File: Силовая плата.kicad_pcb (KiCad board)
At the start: 6 copper layers, 66 x 71.8 mm, 40 parts, among them J3 Conn_01x01, J4 Conn_01x01, J5 Conn_01x01, J6 Conn_01x04, J9 Conn_01x08, Q1 2N7002, Q2 2N7002, Q3 2N7002, Q4 2N7002, Q5 2N7002, Q6 2N7002, U1 AD8210, U2 AD8603, U3 AD8603, U4 AD8603

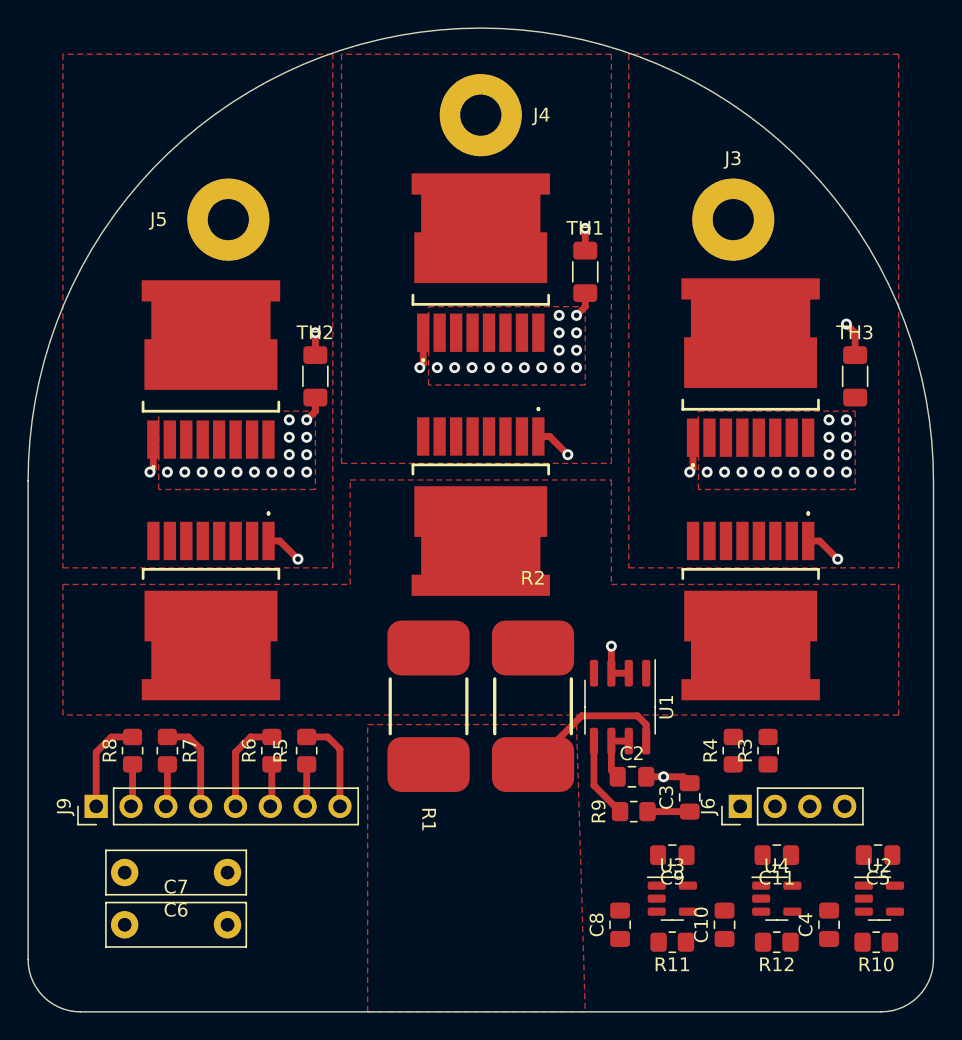
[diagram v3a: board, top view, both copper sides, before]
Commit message: Перенес защиту от переполюсовки и добавил керамику
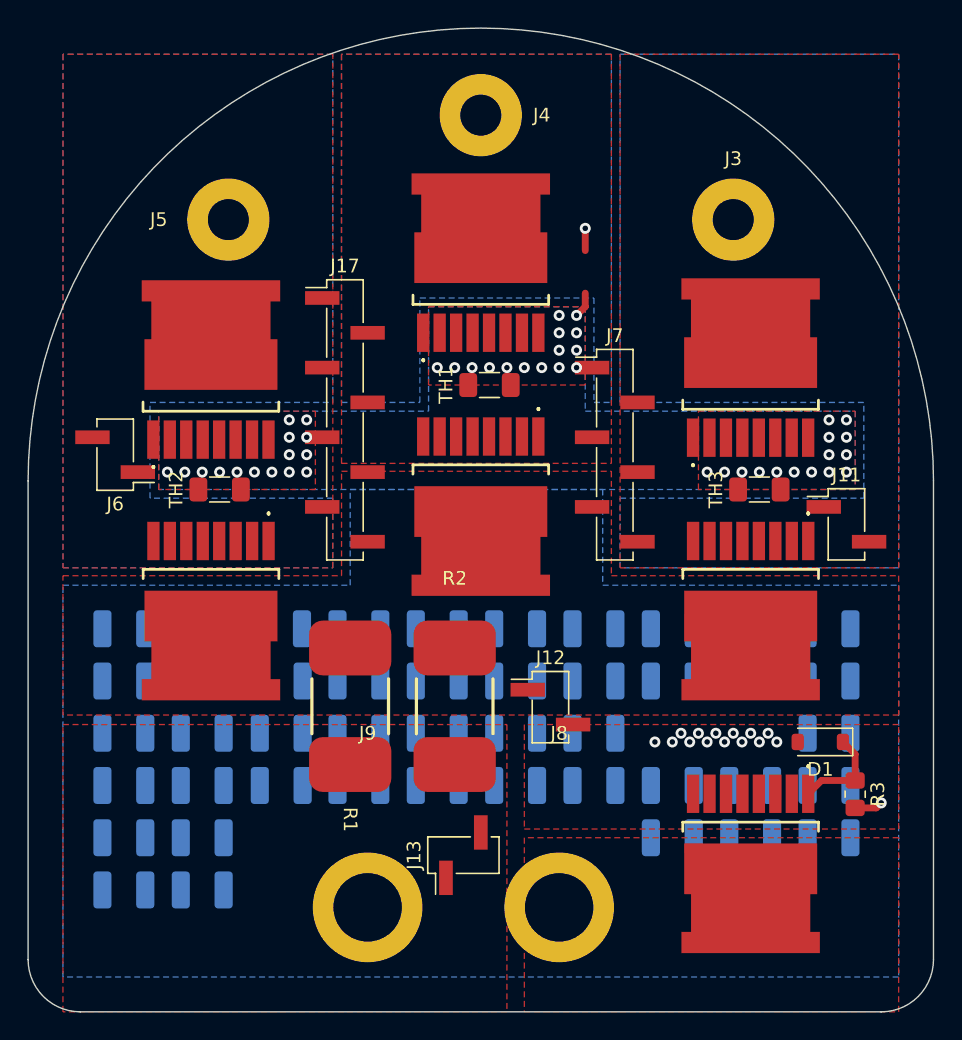
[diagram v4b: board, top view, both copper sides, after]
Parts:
- removed C6, C7: 1500p, Capacitor_THT:C_Rect_L10.0mm_W3.0mm_P7.50mm_FKS3_FKP3
- removed R10, R11, R12, R4, R5, R6, R7, R8: 10k, Resistor_SMD:R_0805_2012Metric_Pad1.20x1.40mm_HandSolder
- removed R9: 120, Resistor_SMD:R_0805_2012Metric_Pad1.20x1.40mm_HandSolder
- removed U1: AD8210, Package_SO:SOIC-8_3.9x4.9mm_P1.27mm
- removed U2, U3, U4: AD8603, Package_TO_SOT_SMD:TSOT-23-5
- added C1: 10u, Capacitor_SMD:C_1210_3225Metric_Pad1.33x2.70mm_HandSolder, B.Cu at (108.6, 120.7)
- added C12: 10u, Capacitor_SMD:C_1210_3225Metric_Pad1.33x2.70mm_HandSolder, B.Cu at (108.6, 116.8)
- added C13: 10u, Capacitor_SMD:C_1210_3225Metric_Pad1.33x2.70mm_HandSolder, B.Cu at (108.6, 109.2)
- added C14: 10u, Capacitor_SMD:C_1210_3225Metric_Pad1.33x2.70mm_HandSolder, B.Cu at (102.9, 109.2)
- added C15: 10u, Capacitor_SMD:C_1210_3225Metric_Pad1.33x2.70mm_HandSolder, B.Cu at (97.2, 120.7)
- added C16: 10u, Capacitor_SMD:C_1210_3225Metric_Pad1.33x2.70mm_HandSolder, B.Cu at (62.9, 124.5)
- added C17: 10u, Capacitor_SMD:C_1210_3225Metric_Pad1.33x2.70mm_HandSolder, B.Cu at (97.2, 109.2)
- added C18: 10u, Capacitor_SMD:C_1210_3225Metric_Pad1.33x2.70mm_HandSolder, B.Cu at (68.6, 105.4)
- added C19: 10u, Capacitor_SMD:C_1210_3225Metric_Pad1.33x2.70mm_HandSolder, B.Cu at (68.6, 109.2)
- added C20: 10u, Capacitor_SMD:C_1210_3225Metric_Pad1.33x2.70mm_HandSolder, B.Cu at (68.6, 113.0)
- added C21: 10u, Capacitor_SMD:C_1210_3225Metric_Pad1.33x2.70mm_HandSolder, B.Cu at (91.4, 109.2)
- added C22: 10u, Capacitor_SMD:C_1210_3225Metric_Pad1.33x2.70mm_HandSolder, B.Cu at (91.4, 105.4)
- added C23: 10u, Capacitor_SMD:C_1210_3225Metric_Pad1.33x2.70mm_HandSolder, B.Cu at (102.9, 105.4)
- added C24: 10u, Capacitor_SMD:C_1210_3225Metric_Pad1.33x2.70mm_HandSolder, B.Cu at (85.7, 105.4)
- added C25: 10u, Capacitor_SMD:C_1210_3225Metric_Pad1.33x2.70mm_HandSolder, B.Cu at (80.0, 105.4)
- added C26: 10u, Capacitor_SMD:C_1210_3225Metric_Pad1.33x2.70mm_HandSolder, B.Cu at (57.1, 124.5)
- added C27: 10u, Capacitor_SMD:C_1210_3225Metric_Pad1.33x2.70mm_HandSolder, B.Cu at (62.9, 116.8)
- added C28: 10u, Capacitor_SMD:C_1210_3225Metric_Pad1.33x2.70mm_HandSolder, B.Cu at (62.9, 113.0)
- added C29: 10u, Capacitor_SMD:C_1210_3225Metric_Pad1.33x2.70mm_HandSolder, B.Cu at (57.1, 120.7)
- added C30: 10u, Capacitor_SMD:C_1210_3225Metric_Pad1.33x2.70mm_HandSolder, B.Cu at (91.4, 116.8)
- added C31: 10u, Capacitor_SMD:C_1210_3225Metric_Pad1.33x2.70mm_HandSolder, B.Cu at (74.3, 113.0)
- added C32: 10u, Capacitor_SMD:C_1210_3225Metric_Pad1.33x2.70mm_HandSolder, B.Cu at (74.3, 116.8)
- added C33: 10u, Capacitor_SMD:C_1210_3225Metric_Pad1.33x2.70mm_HandSolder, B.Cu at (102.9, 116.8)
- added C34: 10u, Capacitor_SMD:C_1210_3225Metric_Pad1.33x2.70mm_HandSolder, B.Cu at (85.7, 116.8)
- added C35: 10u, Capacitor_SMD:C_1210_3225Metric_Pad1.33x2.70mm_HandSolder, B.Cu at (85.7, 113.0)
- added C36: 10u, Capacitor_SMD:C_1210_3225Metric_Pad1.33x2.70mm_HandSolder, B.Cu at (85.7, 109.2)
- added C37: 10u, Capacitor_SMD:C_1210_3225Metric_Pad1.33x2.70mm_HandSolder, B.Cu at (108.6, 105.4)
- added C38: 10u, Capacitor_SMD:C_1210_3225Metric_Pad1.33x2.70mm_HandSolder, B.Cu at (68.6, 116.8)
- added C39: 10u, Capacitor_SMD:C_1210_3225Metric_Pad1.33x2.70mm_HandSolder, B.Cu at (57.1, 116.8)
- added C40: 10u, Capacitor_SMD:C_1210_3225Metric_Pad1.33x2.70mm_HandSolder, B.Cu at (62.9, 105.4)
- added C41: 10u, Capacitor_SMD:C_1210_3225Metric_Pad1.33x2.70mm_HandSolder, B.Cu at (91.4, 113.0)
- added C42: 10u, Capacitor_SMD:C_1210_3225Metric_Pad1.33x2.70mm_HandSolder, B.Cu at (80.0, 113.0)
- added C43: 10u, Capacitor_SMD:C_1210_3225Metric_Pad1.33x2.70mm_HandSolder, B.Cu at (80.0, 116.8)
- added C44: 10u, Capacitor_SMD:C_1210_3225Metric_Pad1.33x2.70mm_HandSolder, B.Cu at (62.9, 120.7)
- added C45: 10u, Capacitor_SMD:C_1210_3225Metric_Pad1.33x2.70mm_HandSolder, B.Cu at (80.0, 109.2)
- added C46: 10u, Capacitor_SMD:C_1210_3225Metric_Pad1.33x2.70mm_HandSolder, B.Cu at (57.1, 113.0)
- added C47: 10u, Capacitor_SMD:C_1210_3225Metric_Pad1.33x2.70mm_HandSolder, B.Cu at (97.2, 105.4)
- added D1: BZT52C10, Diode_SMD:D_SOD-123, F.Cu at (108.0, 113.7)
- added J11: Conn_01x02, Connector_PinHeader_2.54mm:PinHeader_1x02_P2.54mm_Vertical_SMD_Pin1Left, F.Cu at (109.9, 97.8)
- added J12: Conn_01x02, Connector_PinHeader_2.54mm:PinHeader_1x02_P2.54mm_Vertical_SMD_Pin1Left, F.Cu at (88.3, 111.1)
- added J13: Conn_01x02, Connector_PinHeader_2.54mm:PinHeader_1x02_P2.54mm_Vertical_SMD_Pin1Left, F.Cu at (81.9, 121.9)
- added J17: Conn_01x08, Connector_PinHeader_2.54mm:PinHeader_1x08_P2.54mm_Vertical_SMD_Pin1Left, F.Cu at (73.3, 90.2)
- added J7: Conn_01x06, Connector_PinHeader_2.54mm:PinHeader_1x06_P2.54mm_Vertical_SMD_Pin1Left, F.Cu at (93.0, 92.7)
- added J8: IN-, Connector_My:Power_Wire, F.Cu at (88.9, 113.5)
- added Q7: BSS214NW, MOSFET_My:IPTG007N06NM5ATMA1, F.Cu at (102.9, 123.8)
- C10, C11, C4, C5, C8, C9: value 100n -> 10u; footprint Capacitor_SMD:C_0805_2012Metric_Pad1.18x1.45mm_HandSolder -> Capacitor_SMD:C_1210_3225Metric_Pad1.33x2.70mm_HandSolder; moved to B.Cu
- C2: value 0.1u -> 10u; footprint Capacitor_SMD:C_0805_2012Metric_Pad1.18x1.45mm_HandSolder -> Capacitor_SMD:C_1210_3225Metric_Pad1.33x2.70mm_HandSolder; moved to B.Cu
- C3: value 56p -> 10u; footprint Capacitor_SMD:C_0805_2012Metric_Pad1.18x1.45mm_HandSolder -> Capacitor_SMD:C_1210_3225Metric_Pad1.33x2.70mm_HandSolder; moved to B.Cu
- J6: value Conn_01x04 -> Conn_01x02; footprint Connector_PinHeader_2.54mm:PinHeader_1x04_P2.54mm_Vertical -> Connector_PinHeader_2.54mm:PinHeader_1x02_P2.54mm_Vertical_SMD_Pin1Left
- J9: value Conn_01x08 -> IN+; footprint Connector_PinHeader_2.54mm:PinHeader_1x08_P2.54mm_Vertical -> Connector_My:Power_Wire
- R3: value 10k -> 100k
- moved J6 52.3 mm to (56.5, 92.7), turned to 180 degrees
- moved C4 40.5 mm to (74.3, 105.4), turned to 0 degrees
- moved C8 40.3 mm to (57.1, 109.2), turned to 180 degrees
- moved C2 38.6 mm to (57.1, 105.4), turned to 180 degrees
- moved C3 36.6 mm to (62.9, 109.2), turned to 0 degrees
- moved C11 33.0 mm to (74.3, 109.2), turned to 0 degrees
- moved J9 20.4 mm to (74.9, 113.5), turned to 0 degrees
- moved C10 15.9 mm to (108.6, 113.0), turned to 0 degrees
- moved TH1 10.8 mm to (83.8, 87.6), turned to 0 degrees
- moved TH2 10.8 mm to (64.1, 95.2), turned to 0 degrees
- moved TH3 10.8 mm to (103.5, 95.2), turned to 0 degrees
- moved C5 9.38 mm to (102.9, 120.7)
- moved R3 7.10 mm to (110.5, 117.5), turned to -90 degrees
- moved R1 5.72 mm to (73.7, 106.8)
- moved R2 5.72 mm to (81.3, 106.8)
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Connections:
- C10 pad 1: Net-(U4-+) -> Shunt_1
- C11 pad 1: +5V -> Shunt_1
- C2 pad 1: +5V -> Shunt_1
- C3 pad 1: DC_Measure -> Shunt_1
- C4 pad 1: Net-(U2-+) -> Shunt_1
- C5 pad 1: +5V -> Shunt_1
- C8 pad 1: Net-(U3-+) -> Shunt_1
- C9 pad 1: +5V -> Shunt_1
- J6 pad 1: G1 -> G6
- J6 pad 2: A -> GND
- J9 pad 1: G6 -> Shunt_1
- R3 pad 1: A -> Net-(D1-K)
- R3 pad 2: G1 -> Shunt_1
- TH1 pad 1: Net-(U2-+) -> Temp_A
- TH2 pad 1: Net-(U3-+) -> Temp_C
- TH3 pad 1: Net-(U4-+) -> Temp_B
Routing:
- net G4: track 36.5 -> 0.00 mm, vias 1 -> 0
- net G6: track 29.1 -> 0.00 mm, vias 1 -> 0
- net G3: track 25.8 -> 0.00 mm, vias 1 -> 0
- net G2: track 21.8 -> 0.00 mm, vias 1 -> 0
- net G5: track 18.4 -> 0.00 mm, vias 1 -> 0
- net G1: track 15.0 -> 0.00 mm, vias 1 -> 0
- net GND: track 16.6 -> 1.89 mm, vias 47 -> 59
- net Shunt_1: track 11.2 -> 2.06 mm, vias 0 -> 1
- net Net-(D1-K): track 0.00 -> 7.00 mm
- net B: track 6.97 -> 0.00 mm
- net C: track 6.97 -> 0.00 mm
- net Net-(U1-OUT): track 5.93 -> 0.00 mm
- net +5V: track 4.07 -> 0.00 mm
- net DC_Measure: track 3.08 -> 0.00 mm
- net Net-(U4-+): track 2.52 -> 0.00 mm, vias 1 -> 0
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- added copper zone on B.Cu, net A
- added copper zone on B.Cu, net B
- added copper zone on B.Cu, net C
- added copper zone on B.Cu, net GND
- added copper zone on F.Cu, net Net-(J8-Pin_1)

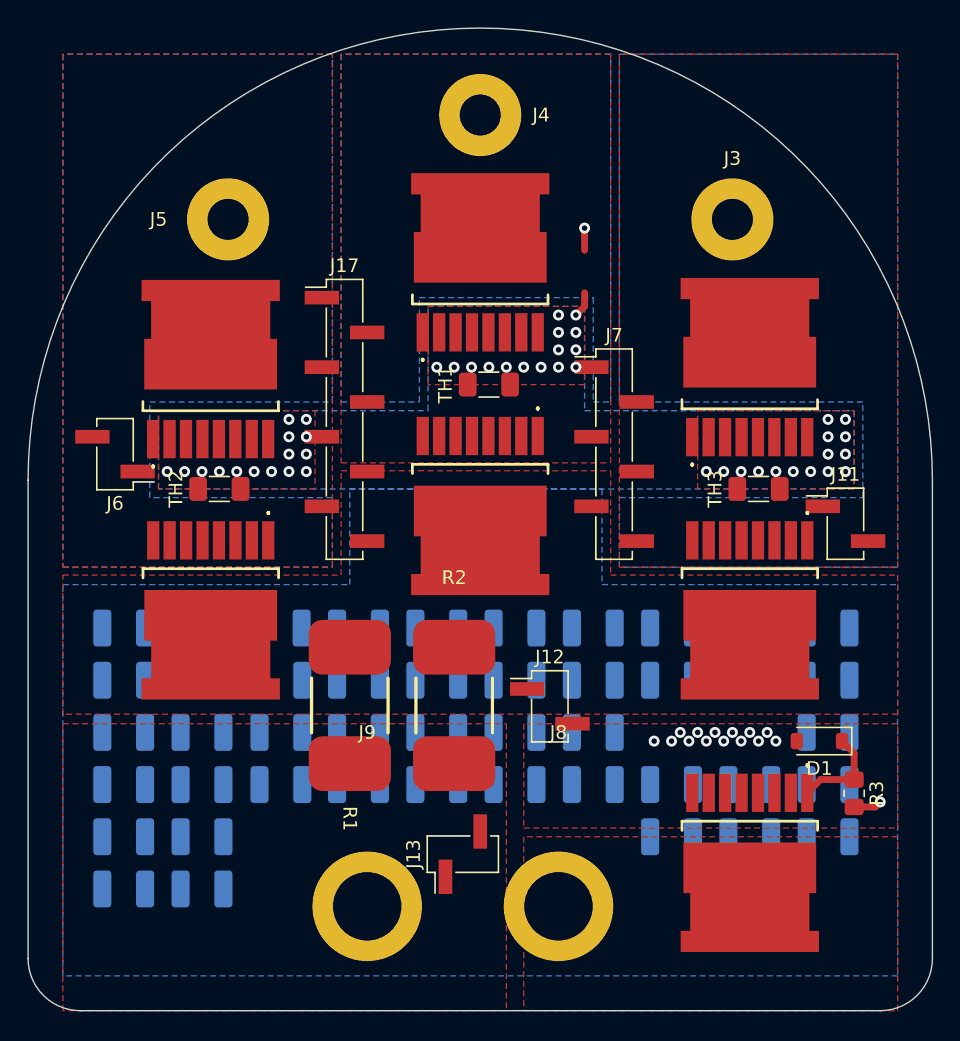
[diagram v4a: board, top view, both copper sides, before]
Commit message: Поставил керамические Y конденсаторы
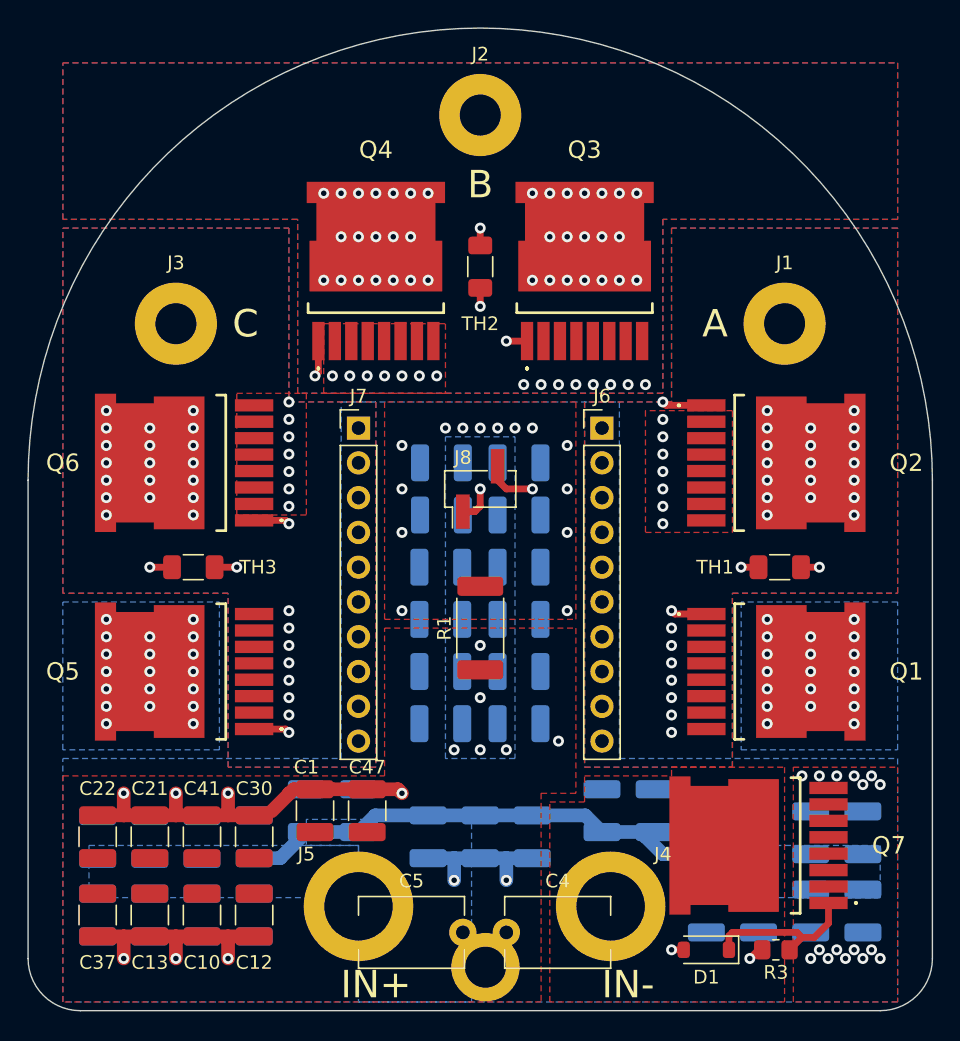
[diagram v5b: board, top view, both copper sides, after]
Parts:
- removed J11, J12: Conn_01x02, Connector_PinHeader_2.54mm:PinHeader_1x02_P2.54mm_Vertical_SMD_Pin1Left
- removed J17: Conn_01x08, Connector_PinHeader_2.54mm:PinHeader_1x08_P2.54mm_Vertical_SMD_Pin1Left
- removed R2: R, Shunt_My:TLRS1050
- added C4: 1500p, Capacitor_THT:C_Disc_D7.5mm_W5.0mm_P7.50mm, F.Cu at (85.1, 127.6)
- added C5: 1500p, Capacitor_THT:C_Disc_D7.5mm_W5.0mm_P7.50mm, F.Cu at (74.4, 127.6)
- added J9: A, Connector_My:Power_Wire, F.Cu at (83.6, 118.0)
- C1, C10, C12, C13, C21, C22, C30, C37, C41, C47: moved to F.Cu
- J1: renamed from J3; value Conn_01x01 -> A
- J2: renamed from J4; value Conn_01x01 -> B
- J3: renamed from J5; value Conn_01x01 -> C
- J6: value Conn_01x02 -> Conn_01x10; footprint Connector_PinHeader_2.54mm:PinHeader_1x02_P2.54mm_Vertical_SMD_Pin1Left -> Connector_PinHeader_2.54mm:PinHeader_1x10_P2.54mm_Vertical
- J7: value Conn_01x06 -> Conn_01x10; footprint Connector_PinHeader_2.54mm:PinHeader_1x06_P2.54mm_Vertical_SMD_Pin1Left -> Connector_PinHeader_2.54mm:PinHeader_1x10_P2.54mm_Vertical
- R1: value R -> PU2512FKGP60U5L; footprint Shunt_My:TLRS1050 -> Resistor_SMD:R_2512_6332Metric_Pad1.40x3.35mm_HandSolder
- moved C37 57.3 mm to (55.2, 126.4), turned to -90 degrees
- moved C13 52.4 mm to (59.1, 126.4), turned to -90 degrees
- moved C10 47.6 mm to (62.9, 126.4), turned to -90 degrees
- moved C12 43.0 mm to (66.7, 126.4), turned to -90 degrees
- moved TH3 41.7 mm to (62.2, 101.0), turned to 180 degrees
- moved C22 39.3 mm to (55.2, 120.7), turned to 90 degrees
- moved C1 37.5 mm to (71.1, 118.7), turned to 90 degrees
- moved J6 35.6 mm to (92.1, 90.8), turned to 0 degrees
- moved C26 35.4 mm to (92.1, 118.7), turned to 90 degrees
- moved C21 34.3 mm to (59.1, 120.7), turned to 90 degrees
- moved C43 32.5 mm to (111.1, 126.1), turned to -90 degrees
- moved C42 30.3 mm to (107.3, 126.1), turned to -90 degrees
- moved C41 29.6 mm to (62.9, 120.7), turned to 90 degrees
- moved C45 28.9 mm to (103.5, 126.1), turned to -90 degrees
- moved C9 28.9 mm to (80.4, 93.3), turned to 180 degrees
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- renumbered C4 to C6, C5 to C7, J8 to J4, J9 to J5, J13 to J8
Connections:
- J6 pad 1: G6 -> B
- J6 pad 2: GND -> G3
- J7 pad 1: G3 -> Temp_B
- J7 pad 2: B -> GND
- J7 pad 3: G2 -> GND
- J7 pad 4: GND -> G4
- J7 pad 5: Temp_A -> GND
- J7 pad 6: GND -> G6
- TH2 pad 1: Temp_C -> Temp_B
- TH3 pad 1: Temp_B -> Temp_C
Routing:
- net GND: track 1.89 -> 152.0 mm, vias 59 -> 51
- net Shunt_1: track 2.06 -> 46.5 mm, vias 1 -> 8
- net Temp_B: track 0.00 -> 15.8 mm, vias 0 -> 1
- net G3: track 0.00 -> 15.6 mm, vias 0 -> 1
- net G4: track 0.00 -> 15.4 mm, vias 0 -> 1
- net Temp_C: track 0.00 -> 12.6 mm, vias 0 -> 1
- net G2: track 0.00 -> 12.1 mm, vias 0 -> 1
- net G6: track 0.00 -> 11.2 mm, vias 0 -> 1
- net Temp_A: track 1.62 -> 11.4 mm
- net G1: track 0.00 -> 8.52 mm, vias 0 -> 1
- net Shunt_2: track 0.00 -> 8.04 mm, vias 0 -> 71
- net G5: track 0.00 -> 7.99 mm, vias 0 -> 1
- net B: track 0.00 -> 7.03 mm, vias 0 -> 27
- net A: track 0.00 -> 6.40 mm, vias 0 -> 26
- net C: track 0.00 -> 5.34 mm, vias 0 -> 26
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- added copper zone on In4.Cu, net A
- added copper zone on In4.Cu, net B
- added copper zone on In4.Cu, net C
- added copper zone on In1.Cu, net GND
- added copper zone on B.Cu, net Shunt_1
- added copper zone on In3.Cu, net Shunt_1
- added copper zone on B.Cu, net Shunt_2
- added copper zone on In3.Cu, net Shunt_2
